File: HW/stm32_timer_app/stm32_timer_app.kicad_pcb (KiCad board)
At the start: 2 copper layers, 107 x 72 mm, 20 parts, among them J1 105164-0001, J2 61300411121, Q1 BTA10-600BRG, U1 RT9193-33GB, U2 MOC3041SM, U3 STM32F103C8T6

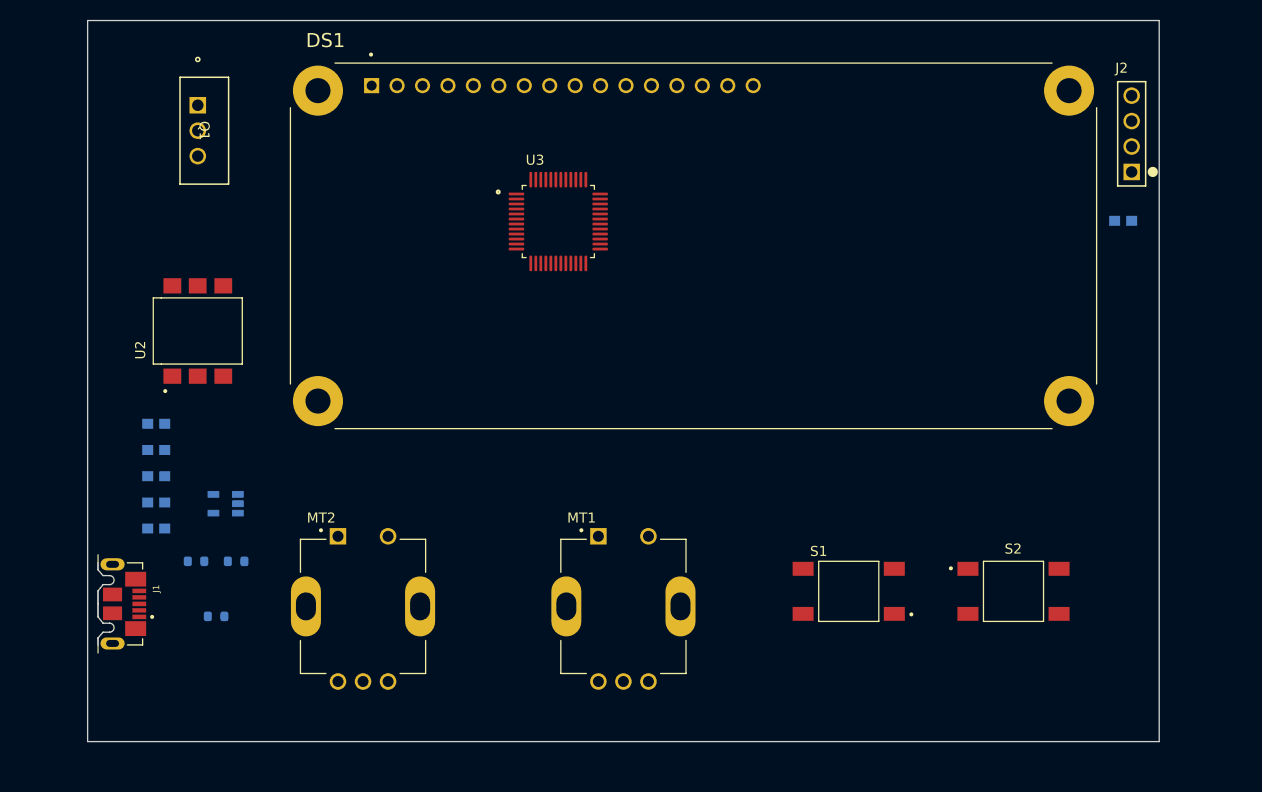
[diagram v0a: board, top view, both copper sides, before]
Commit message: schematic design
added schematic for 3v3 regulator, reset switch, micro USB and two led
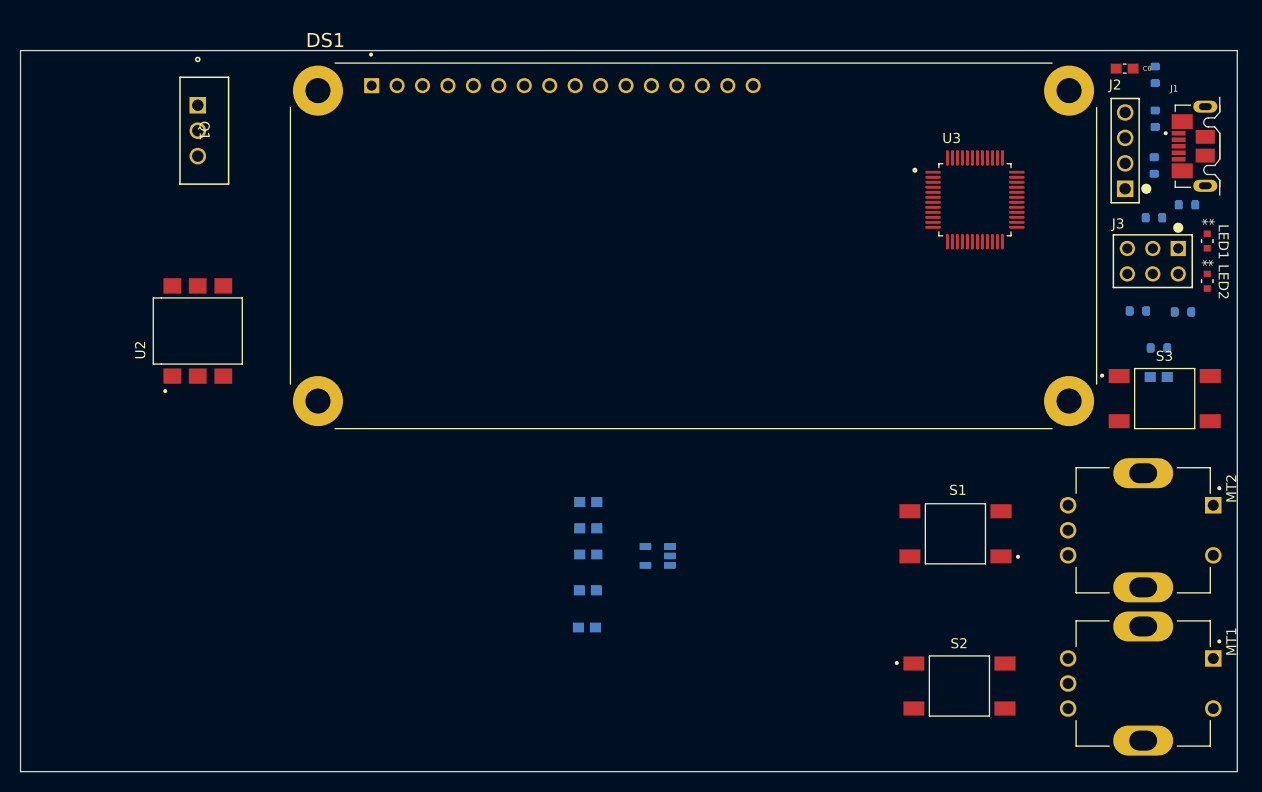
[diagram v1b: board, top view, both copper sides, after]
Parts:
- added C7: 105, LD03ZD475MAB2A:CAPC1608X90, B.Cu at (250.9, 53.6)
- added J3: PH2-06-UA, PH2_06_UA:CONN_PH2-06-UA_ADM, F.Cu at (252.9, 40.8)
- added LED1: 150060GS75000, 150060GS75000:LED_150060GS75000_WRE, F.Cu at (255.8, 40.0)
- added LED2: 150060GS75000, 150060GS75000:LED_150060GS75000_WRE, F.Cu at (255.8, 44.0)
- added R4: 10K, Resistor_SMD:R_0603_1608Metric, B.Cu at (251.0, 50.7)
- added R5: 100K, Resistor_SMD:R_0603_1608Metric, B.Cu at (250.5, 37.7)
- added R6: 100K, Resistor_SMD:R_0603_1608Metric, B.Cu at (248.9, 47.0)
- added R7: 100K, Resistor_SMD:R_0603_1608Metric, B.Cu at (253.8, 36.4)
- added R8: 100K, Resistor_SMD:R_0603_1608Metric, B.Cu at (253.4, 47.1)
- added S3: 1571527-1, 1571527-1:SW_1571527-1, F.Cu at (251.6, 55.8)
- C6: moved to F.Cu
- moved J1 121.0 mm to (257.1, 30.6), turned to 90 degrees
- moved R3 107.4 mm to (250.6, 23.4), turned to -90 degrees
- moved R1 103.9 mm to (250.5, 32.5), turned to -90 degrees
- moved R2 101.9 mm to (250.6, 27.8), turned to 90 degrees
- moved MT2 78.3 mm to (249.4, 68.9), turned to -90 degrees
- moved MT1 52.5 mm to (249.4, 84.2), turned to -90 degrees
- moved C2 47.6 mm to (193.8, 78.6)
- moved C1 43.5 mm to (193.9, 74.9)
- moved C3 43.5 mm to (194.0, 66.1)
- moved C4 43.5 mm to (194.0, 68.7)
- moved C5 43.5 mm to (194.0, 71.3)
- moved U1 43.5 mm to (200.9, 71.5)
- moved U3 41.7 mm to (232.6, 35.9)
- moved C6 15.2 mm to (247.6, 22.8), turned to 0 degrees
- moved S1 12.1 mm to (230.7, 69.2)
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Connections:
- net +3.3V renamed Net-(U1-VOUT)
- C1 pad 1: GNDREF -> Net-(C1-Pad1)
- C1 pad 2: +5V -> Net-(U1-EN)
- C2 pad 1: GNDREF -> Net-(C1-Pad1)
- C2 pad 2: +5V -> Net-(U1-EN)
- C3 pad 1: GNDREF -> Net-(U1-GND)
- C4 pad 1: GNDREF -> Net-(U1-GND)
- C5 pad 1: GNDREF -> Net-(U1-GND)
- C6 pad 1: VCC3V3 -> Net-(C6-Pad1)
- C6 pad 2: GNDREF -> Net-(C6-Pad2)
- DS1 pad 16: (no net) -> unconnected-(DS1-VEE-Pad16)
- J1 pad 1: GNDREF -> Net-(J1-G)
- J1 pad 2: GNDREF -> Net-(J1-G)
- J1 pad 5: +5V -> Net-(J1-Vbus)
- J1 pad SH1: GNDREF -> Net-(J1-SHIELD-PadSH1)
- J1 pad SH2: GNDREF -> Net-(J1-SHIELD-PadSH1)
- J1 pad SH3: GNDREF -> Net-(J1-SHIELD-PadSH1)
- J1 pad SH4: GNDREF -> Net-(J1-SHIELD-PadSH1)
- J1 pad SH5: GNDREF -> Net-(J1-SHIELD-PadSH1)
- J1 pad SH6: GNDREF -> Net-(J1-SHIELD-PadSH1)
- J2 pad 1: VCC3V3 -> Net-(C6-Pad1)
- J2 pad 4: GNDREF -> Net-(C6-Pad2)
- R3 pad 1: +5V -> Net-(R3-Pad1)
- U1 pad 1: +5V -> Net-(U1-EN)
- U1 pad 2: GNDREF -> Net-(U1-GND)
- U1 pad 3: +5V -> Net-(U1-EN)
- U2 pad 3: (no net) -> unconnected-(U2-Pad3)
- U2 pad 5: (no net) -> unconnected-(U2-Pad5)
- U3 pad 2: unconnected-(U3-PC13-TAMPER-RTC-Pad2) -> PC13
- U3 pad 20: unconnected-(U3-PB2-Pad20) -> BOOT1
- U3 pad 23: Net-(U3-VSS-Pad23) -> unconnected-(U3-VSS-Pad23)
- U3 pad 24: VCC3V3 -> Net-(U3-VDD-Pad24)
- U3 pad 35: Net-(U3-VSS-Pad23) -> unconnected-(U3-VSS-Pad35)
- U3 pad 36: VCC3V3 -> unconnected-(U3-VDD-Pad36)
- U3 pad 44: unconnected-(U3-BOOT0-Pad44) -> BOOT0
- U3 pad 47: Net-(U3-VSS-Pad23) -> unconnected-(U3-VSS-Pad47)
- U3 pad 48: VCC3V3 -> unconnected-(U3-VDD-Pad48)
- U3 pad 7: unconnected-(U3-NRST-Pad7) -> RESET
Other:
- board size 107 x 72 mm -> 121.5 x 72 mm

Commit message: schematic design
schematic design revision 1
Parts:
- added C10: 104, LD03ZD475MAB2A:CAPC1608X90, B.Cu at (239.0, 48.1)
- added C11: 104, LD03ZD475MAB2A:CAPC1608X90, B.Cu at (239.0, 50.7)
- added C12: 20p, LD03ZD475MAB2A:CAPC1608X90, B.Cu at (249.2, 51.9)
- added C13: 20p, LD03ZD475MAB2A:CAPC1608X90, B.Cu at (253.6, 51.9)
- added C14: 20p, LD03ZD475MAB2A:CAPC1608X90, F.Cu at (240.8, 37.4)
- added C15: 20p, LD03ZD475MAB2A:CAPC1608X90, F.Cu at (242.6, 34.7)
- added C16: ECW-FD2J273KQ, ECW_FD2J273KQ:CAP_ECWFD_FORMINGQ_12.6LX06.9TX09.9H_PAN, F.Cu at (198.9, 83.5)
- added C8: 104, LD03ZD475MAB2A:CAPC1608X90, B.Cu at (239.0, 42.9)
- added C9: 104, LD03ZD475MAB2A:CAPC1608X90, B.Cu at (239.0, 45.5)
- added CR1: 1N4148W-13-F, 1N4148W_13_F:SOD123_DIO, B.Cu at (235.3, 89.7)
- added CR2: 1N4148W-13-F, 1N4148W_13_F:SOD123_DIO, B.Cu at (235.6, 80.1)
- added CR3: 1N4148W-13-F, 1N4148W_13_F:SOD123_DIO, B.Cu at (228.8, 85.1)
- added CR4: 1N4148W-13-F, 1N4148W_13_F:SOD123_DIO, B.Cu at (236.0, 73.7)
- added CR5: 1N4148W-13-F, 1N4148W_13_F:SOD123_DIO, B.Cu at (236.2, 63.6)
- added CR6: 1N4148W-13-F, 1N4148W_13_F:SOD123_DIO, B.Cu at (229.0, 68.5)
- added J4: 691213710002, 691213710002:691213710002, F.Cu at (168.6, 67.6)
- added J5: 691213710002, 691213710002:691213710002, F.Cu at (170.0, 82.9)
- added R10: 10K, Resistor_SMD:R_0603_1608Metric, B.Cu at (235.4, 87.3)
- added R11: 10K, Resistor_SMD:R_0603_1608Metric, B.Cu at (235.6, 77.9)
- added R12: 10K, Resistor_SMD:R_0603_1608Metric, B.Cu at (228.8, 82.6)
- added R13: 10K, Resistor_SMD:R_0603_1608Metric, B.Cu at (236.1, 61.2)
- added R14: 10K, Resistor_SMD:R_0603_1608Metric, B.Cu at (236.0, 71.3)
- added R15: 10K, Resistor_SMD:R_0603_1608Metric, B.Cu at (228.9, 65.9)
- added R16: 10K, Resistor_SMD:R_0603_1608Metric, B.Cu at (228.7, 89.9)
- added R17: 10K, Resistor_SMD:R_0603_1608Metric, B.Cu at (228.7, 77.9)
- added R18: 10K, Resistor_SMD:R_0603_1608Metric, B.Cu at (223.1, 84.8)
- added R19: 10K, Resistor_SMD:R_0603_1608Metric, B.Cu at (228.7, 72.5)
- added R20: 10K, Resistor_SMD:R_0603_1608Metric, B.Cu at (228.8, 60.8)
- added R21: 10K, Resistor_SMD:R_0603_1608Metric, B.Cu at (223.2, 68.4)
- added R22: TC33X-2-102E, TC33X_2_102E:TRIM_TC33X-2-102E, F.Cu at (213.7, 65.2)
- added R23: 220, Resistor_SMD:R_0603_1608Metric, F.Cu at (227.0, 77.3)
- added R24: 220, Resistor_SMD:R_0603_1608Metric, F.Cu at (217.0, 77.4)
- added R25: 1K, Resistor_SMD:R_0603_1608Metric, F.Cu at (219.3, 62.7)
- added R26: 360, Resistor_SMD:R_0603_1608Metric, F.Cu at (209.0, 72.3)
- added R27: 330, Resistor_SMD:R_0603_1608Metric, F.Cu at (196.9, 60.6)
- added R29: 39, OY390KE:RES_OY_OHM, F.Cu at (181.2, 90.5)
- added R9: 20R, Resistor_SMD:R_0603_1608Metric, B.Cu at (251.6, 46.2)
- added Y1: ABL-8.000MHZ-B2, ABL-8.000MHZ-B2:XTAL_HC49P488W46L1150T500H350, F.Cu at (251.5, 48.7)
- added Y2: ABS25-32.768KHZ-6-4-T, ABS25-32.768KHZ-6-4-T:XTAL_ABS25-32.768KHZ-6-4-T, F.Cu at (241.6, 43.8)
- moved U2 75.9 mm to (228.7, 67.4), turned to 0 degrees
- moved C2 63.7 mm to (243.1, 38.1)
- moved C1 62.8 mm to (243.1, 35.7)
- moved Q1 60.1 mm to (200.8, 65.4), turned to 180 degrees
- moved C4 58.0 mm to (237.7, 30.6), turned to -90 degrees
- moved C5 57.3 mm to (234.3, 30.6), turned to -90 degrees
- moved U1 52.9 mm to (239.0, 34.8)
- moved C3 50.8 mm to (234.7, 35.7), turned to 0 degrees
- moved S2 17.8 mm to (213.2, 83.5)
- moved S1 14.1 mm to (229.2, 83.3)
- moved R6 13.7 mm to (238.6, 38.0)
- moved U3 8.11 mm to (231.0, 43.9), turned to 180 degrees
- moved R4 7.17 mm to (257.5, 47.7), turned to 90 degrees
- moved R8 6.23 mm to (257.5, 42.4), turned to -90 degrees
- moved C7 1.17 mm to (251.3, 54.7)
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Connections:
- C1 pad 2: Net-(U1-EN) -> +5V
- C2 pad 2: Net-(U1-EN) -> +5V
- C4 pad 2: Net-(U1-VOUT) -> PA3
- C5 pad 2: Net-(U1-VOUT) -> PA3
- C6 pad 1: Net-(C6-Pad1) -> PA3
- DS1 pad 1: unconnected-(DS1-VSS-Pad1) -> Net-(DS1-VSS)
- DS1 pad 10: unconnected-(DS1-DB3-Pad10) -> Net-(DS1-DB0)
- DS1 pad 11: unconnected-(DS1-DB4-Pad11) -> PB3
- DS1 pad 12: unconnected-(DS1-DB5-Pad12) -> PB4
- DS1 pad 13: unconnected-(DS1-DB6-Pad13) -> PB5
- DS1 pad 14: unconnected-(DS1-DB7-Pad14) -> PB6
- DS1 pad 15: unconnected-(DS1-VEE-Pad15) -> +5V
- DS1 pad 16: unconnected-(DS1-VEE-Pad16) -> Net-(DS1-DB0)
- DS1 pad 2: unconnected-(DS1-VDD-Pad2) -> +5V
- DS1 pad 3: unconnected-(DS1-VO-Pad3) -> Net-(DS1-VO)
- DS1 pad 4: unconnected-(DS1-RS-Pad4) -> PB1
- DS1 pad 5: unconnected-(DS1-R/~{W}-Pad5) -> Net-(DS1-R/~{W})
- DS1 pad 6: unconnected-(DS1-E-Pad6) -> PB0
- DS1 pad 7: unconnected-(DS1-DB0-Pad7) -> Net-(DS1-DB0)
- DS1 pad 8: unconnected-(DS1-DB1-Pad8) -> Net-(DS1-DB0)
- DS1 pad 9: unconnected-(DS1-DB2-Pad9) -> Net-(DS1-DB0)
- DS1 pad S1: Net-(DS1-SHIELD-PadS1) -> unconnected-(DS1-SHIELD-PadS1)
- DS1 pad S2: Net-(DS1-SHIELD-PadS1) -> unconnected-(DS1-SHIELD-PadS2)
- DS1 pad S3: Net-(DS1-SHIELD-PadS1) -> unconnected-(DS1-SHIELD-PadS3)
- DS1 pad S4: Net-(DS1-SHIELD-PadS1) -> unconnected-(DS1-SHIELD-PadS4)
- J1 pad 5: Net-(J1-Vbus) -> +5V
- J2 pad 1: Net-(C6-Pad1) -> PA3
- J3 pad 5: Net-(J3-Pad5) -> PA3
- J3 pad 6: Net-(J3-Pad5) -> PA3
- LED1 pad 2: Net-(LED1-Pad2) -> PA3
- LED2 pad 2: Net-(LED1-Pad2) -> PA3
- MT1 pad 1: unconnected-(MT1-Pad1) -> Net-(MT1-Pad1)
- MT1 pad 2: unconnected-(MT1-Pad2) -> Net-(CR1-Pad2)
- MT1 pad A: unconnected-(MT1-PadA) -> Net-(CR2-Pad2)
- MT1 pad B: unconnected-(MT1-PadB) -> Net-(CR3-Pad2)
- MT1 pad COM: unconnected-(MT1-PadCOM) -> Net-(MT1-Pad1)
- MT1 pad S1: Net-(MT1-SHIELD-PadS1) -> Net-(MT1-Pad1)
- MT1 pad S2: Net-(MT1-SHIELD-PadS1) -> Net-(MT1-Pad1)
- MT2 pad 1: unconnected-(MT2-Pad1) -> Net-(MT2-Pad1)
- MT2 pad 2: unconnected-(MT2-Pad2) -> Net-(CR4-Pad2)
- MT2 pad A: unconnected-(MT2-PadA) -> Net-(CR5-Pad2)
- MT2 pad B: unconnected-(MT2-PadB) -> Net-(CR6-Pad2)
- MT2 pad COM: unconnected-(MT2-PadCOM) -> Net-(MT2-Pad1)
- MT2 pad S1: Net-(MT2-SHIELD-PadS1) -> Net-(MT2-Pad1)
- MT2 pad S2: Net-(MT2-SHIELD-PadS1) -> Net-(MT2-Pad1)
- Q1 pad 1: unconnected-(Q1-A1-Pad1) -> Net-(Q1-A1)
- Q1 pad 2: unconnected-(Q1-A2-Pad2) -> Net-(Q1-A2)
- Q1 pad 3: unconnected-(Q1-G-Pad3) -> Net-(Q1-G)
- R3 pad 1: Net-(R3-Pad1) -> +5V
- R4 pad 2: Net-(R4-Pad2) -> PA3
- S1 pad 3: Net-(S1-Pad3) -> PA3
- S1 pad 4: Net-(S1-Pad3) -> PA3
- S2 pad 3: Net-(S2-Pad3) -> PA3
- S2 pad 4: Net-(S2-Pad3) -> PA3
- U1 pad 1: Net-(U1-EN) -> +5V
- U1 pad 3: Net-(U1-EN) -> +5V
- U1 pad 5: Net-(U1-VOUT) -> PA3
- U2 pad 1: unconnected-(U2-Pad1) -> Net-(R25-Pad2)
- U2 pad 2: unconnected-(U2-Pad2) -> Net-(U2-Pad2)
- U2 pad 4: unconnected-(U2-Pad4) -> Net-(Q1-G)
- U2 pad 6: unconnected-(U2-Pad6) -> Net-(R26-Pad1)
- U3 pad 10: unconnected-(U3-PA0_WKUP-Pad10) -> PA0
- U3 pad 11: unconnected-(U3-PA1-Pad11) -> PA1
- U3 pad 12: unconnected-(U3-PA2-Pad12) -> PA2
- U3 pad 13: unconnected-(U3-PA3-Pad13) -> PA3
- U3 pad 14: unconnected-(U3-PA4-Pad14) -> PA3
- U3 pad 15: unconnected-(U3-PA5-Pad15) -> PA5
- U3 pad 16: unconnected-(U3-PA6-Pad16) -> PA6
- U3 pad 17: unconnected-(U3-PA7-Pad17) -> PA7
- U3 pad 18: unconnected-(U3-PB0-Pad18) -> PB0
- U3 pad 19: unconnected-(U3-PB1-Pad19) -> PB1
- U3 pad 24: Net-(U3-VDD-Pad24) -> PA3
- U3 pad 3: unconnected-(U3-PC14-OSC32_IN-Pad3) -> PC14
- U3 pad 36: unconnected-(U3-VDD-Pad36) -> PA3
- U3 pad 39: unconnected-(U3-PB3-Pad39) -> PB3
- U3 pad 4: unconnected-(U3-PC15-OSC32_OUT-Pad4) -> PC15
- U3 pad 40: unconnected-(U3-PB4-Pad40) -> PB4
- U3 pad 41: unconnected-(U3-PB5-Pad41) -> PB5
- U3 pad 42: unconnected-(U3-PB6-Pad42) -> PB6
- U3 pad 43: unconnected-(U3-PB7-Pad43) -> PB7
- U3 pad 48: unconnected-(U3-VDD-Pad48) -> PA3
- U3 pad 5: unconnected-(U3-PD0_OSC_IN-Pad5) -> OSCIN
- U3 pad 6: unconnected-(U3-PD1_OSC_OUT-Pad6) -> OSCOUT
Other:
- board size 121.5 x 72 mm -> 96.1 x 71.9 mm
- board text added: "AC IN"
- board text added: "LOAD"
- board text added: "OFF TIME"
- board text added: "ON TIME"
- board text added: "RESET"
- board text added: "RESTART"
- board text added: "START"

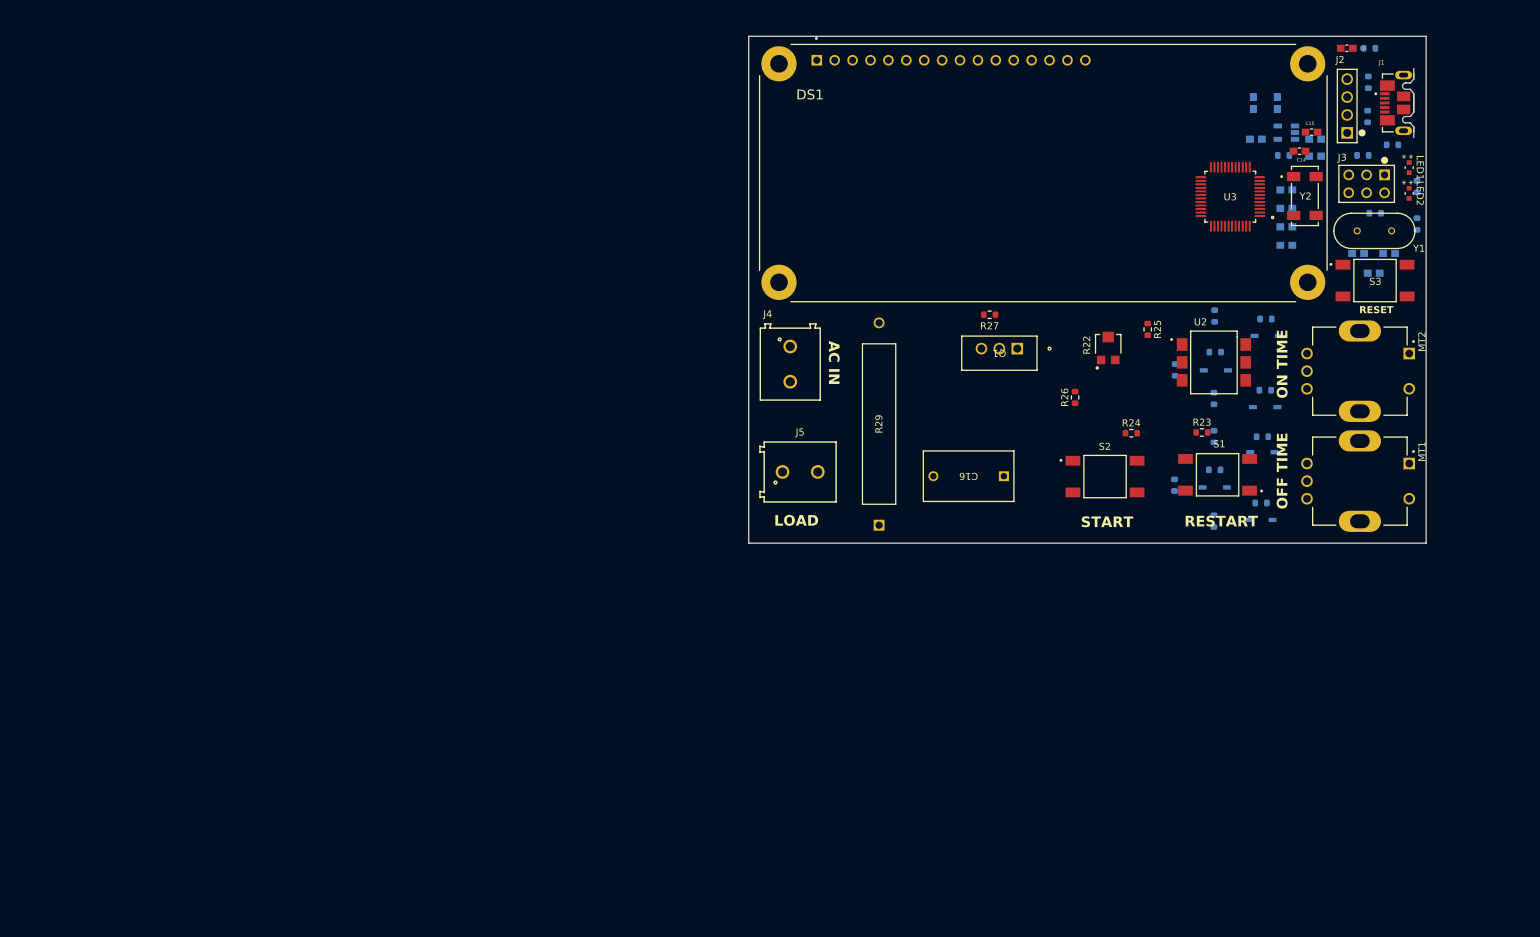
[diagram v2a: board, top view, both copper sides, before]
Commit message: replace 16x2 lcd with 2.4" OLED foot print
replace 16x2 lcd with 2.4" OLED foot print
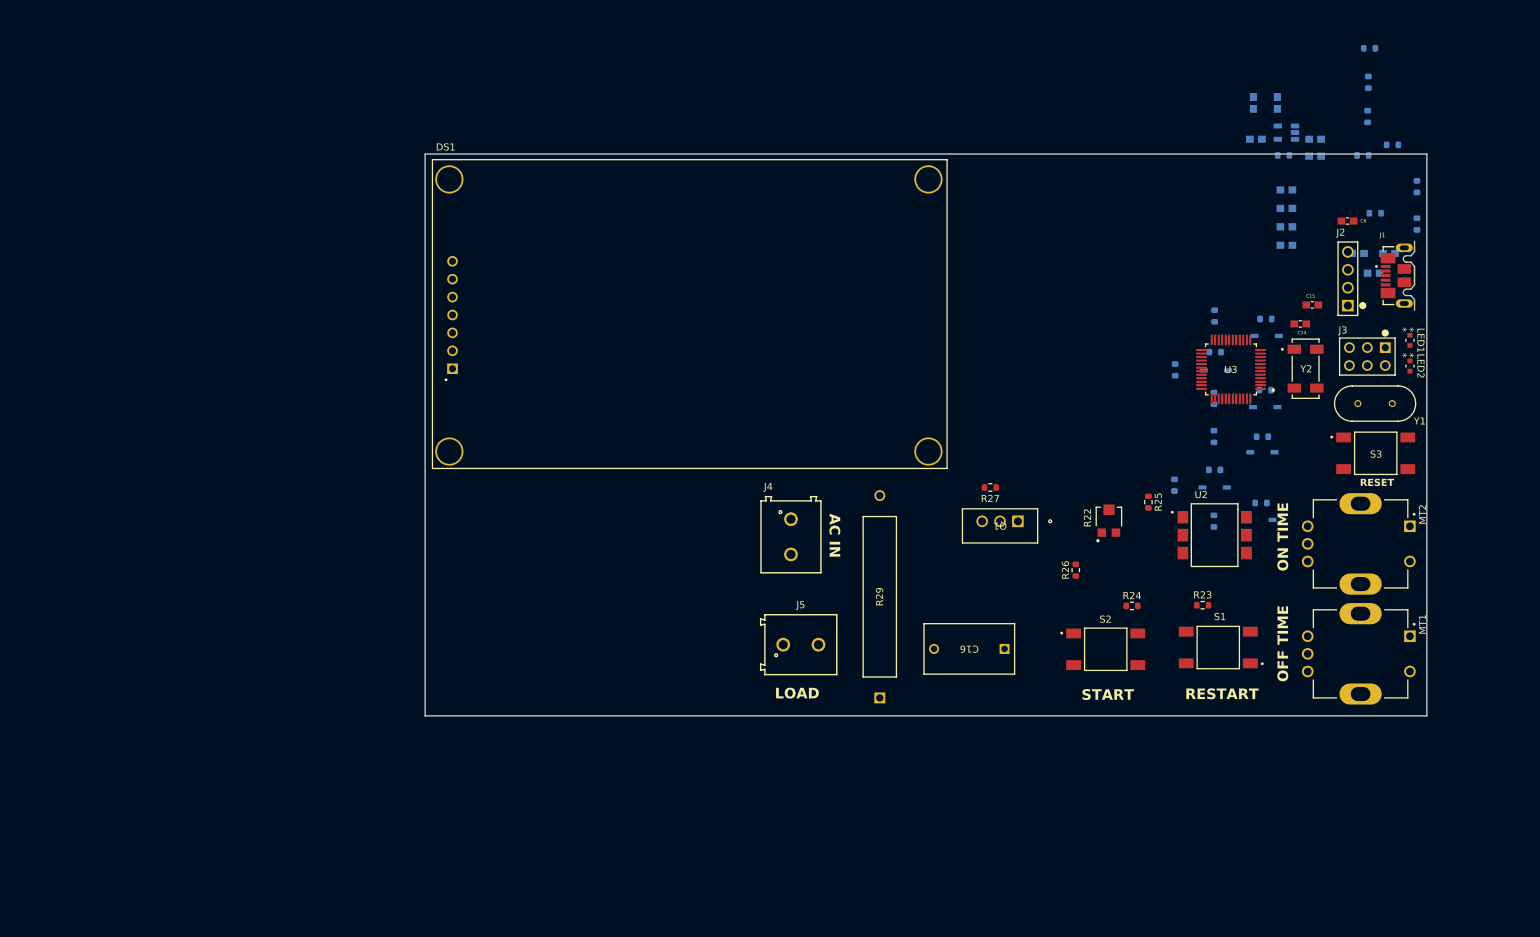
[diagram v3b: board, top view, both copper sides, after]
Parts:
- DS1: value RC1602B-BIW-CSV -> AOM12864A0-1.54WW-ANO; footprint RC1602B-BIW-CSV:LCD_RC1602B-BIW-CSV -> AOM12864A0-1.54WW-ANO:LCD_AOM12864A0-1.54WW-ANO
- moved DS1 96.3 mm to (117.8, 82.4)
- moved J3 24.5 mm to (253.0, 65.3)
- moved C14 24.5 mm to (240.9, 61.9)
- moved C15 24.5 mm to (242.7, 59.2)
- moved C16 24.5 mm to (199.0, 108.0)
- moved J2 24.5 mm to (247.7, 59.3)
- moved J4 24.5 mm to (168.7, 92.1)
- moved J5 24.5 mm to (170.1, 107.4)
- moved LED1 24.5 mm to (256.5, 64.2)
- moved MT1 24.5 mm to (249.5, 108.7)
- moved MT2 24.5 mm to (249.5, 93.1)
- moved Q1 24.5 mm to (200.9, 89.9)
- moved R22 24.5 mm to (213.8, 89.7)
- moved R23 24.5 mm to (227.1, 101.8)
- moved R24 24.5 mm to (217.1, 101.9)
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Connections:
- DS1 pad 1: Net-(DS1-VSS) -> unconnected-(DS1-GND-Pad1)
- DS1 pad 2: +5V -> unconnected-(DS1-VDD-Pad2)
- DS1 pad 3: Net-(DS1-VO) -> unconnected-(DS1-SCL-Pad3)
- DS1 pad 4: PB1 -> unconnected-(DS1-SDA-Pad4)
- DS1 pad 5: Net-(DS1-R/~{W}) -> unconnected-(DS1-RST-Pad5)
- DS1 pad 6: PB0 -> unconnected-(DS1-DC-Pad6)
- DS1 pad 7: Net-(DS1-DB0) -> unconnected-(DS1-CS-Pad7)
- U3 pad 18: PB0 -> unconnected-(U3-PB0-Pad18)
- U3 pad 19: PB1 -> unconnected-(U3-PB1-Pad19)
- U3 pad 39: PB3 -> unconnected-(U3-PB3-Pad39)
- U3 pad 40: PB4 -> unconnected-(U3-PB4-Pad40)
- U3 pad 41: PB5 -> unconnected-(U3-PB5-Pad41)
- U3 pad 42: PB6 -> unconnected-(U3-PB6-Pad42)
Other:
- board size 96.1 x 71.9 mm -> 142.1 x 79.7 mm
